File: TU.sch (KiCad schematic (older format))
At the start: 5 parts, among them J1 Conn_01x06_Male, J2 Conn_01x17_Male, J3 Conn_Coaxial, J4 Debugger connector, J7 Conn_Coaxial

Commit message: More routing changes
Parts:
- removed J3, J7: Conn_Coaxial, Connector_Coaxial:SMA_Amphenol_132134-10_Vertical, symbol Connector:Conn_Coaxial
- added J3, J6: Conn_01x05_Male, TU-HW RF LIB:Wurth_SMA_60312002114503, symbol Connector:Conn_01x05_Male
- added R18: 0, Resistor_SMD:R_0603_1608Metric, symbol Device:R
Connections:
- net +5V: now also R18.1; no longer J2.5 (Pin_5)
- net CC1190/ANTENNA_OUT: now also J3.1 (Pin_1)
- net GND: now also J2.17 (Pin_17), J3.2 (Pin_2), J3.3 (Pin_3), J3.4 (Pin_4), J3.5 (Pin_5), J6.2 (Pin_2), J6.3 (Pin_3), J6.4 (Pin_4), J6.5 (Pin_5)
- net GPIO2: now reaches J4.3 (Pin_3)
- net GPIO0: now reaches J4.4 (Pin_4)
- net at J2.1 (Pin_1): now also J6.1 (Pin_1)
- net ~RESET_RF2: now reaches J2.14 (Pin_14)
- net DIO5: now reaches J2.15 (Pin_15)
- net DIO3: now reaches J2.3 (Pin_3)
- net DIO4: now reaches J2.4 (Pin_4)
- net DIO0: now reaches J2.6 (Pin_6)
- net DIO1: now reaches J2.7 (Pin_7)
- net DIO2: now reaches J2.8 (Pin_8)
- net MCU/MISO renamed MISO
- net MISO: no longer J2.10 (Pin_10)
- net MCU/MOSI renamed MOSI
- net MOSI: no longer J2.11 (Pin_11)
- net MCU/SLCK renamed SCLK
- net SCLK: no longer J2.12 (Pin_12)
- net MCU/~CS_2 renamed ~CS_1
- net ~CS_1: no longer J2.13 (Pin_13)
- net transceiver/~RESET renamed ~RESET
- new net: J2.5 (Pin_5), R18.2
- new net MISO_RF2: J2.10 (Pin_10)
- new net MOSI_RF2: J2.11 (Pin_11)
- new net SCLK_RF2: J2.12 (Pin_12)
- new net ~CS_RF2: J2.13 (Pin_13)
- no-connect marks 10 -> 1
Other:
- note removed: "Piggyback backup rf module"
- moved on the sheet: J2

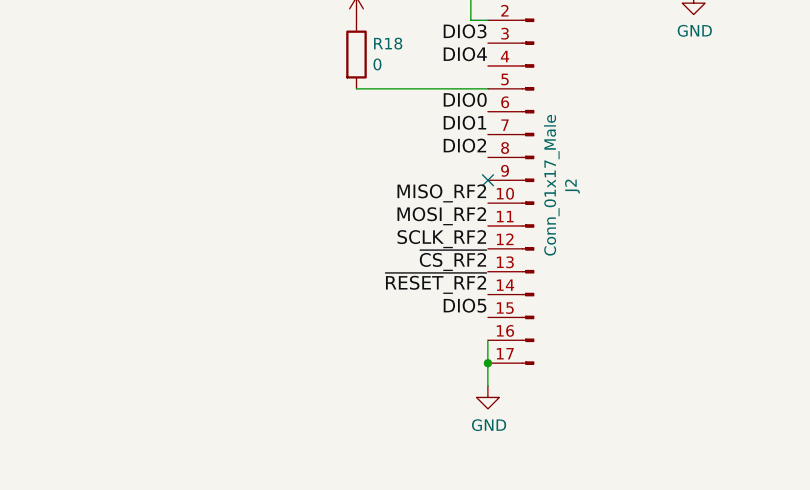
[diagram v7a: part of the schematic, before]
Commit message: Added edge cuts and silk screen comments
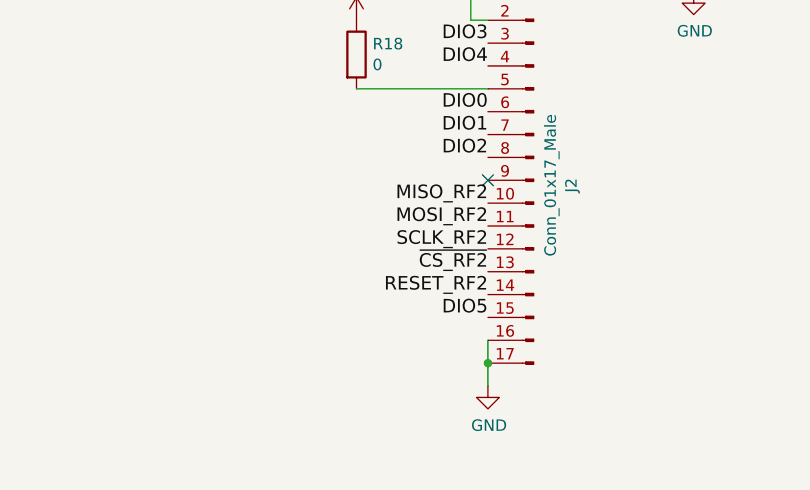
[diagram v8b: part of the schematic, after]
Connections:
- net ~RESET_RF2 is gone; now on net RESET_RF2: J2.14 (Pin_14)
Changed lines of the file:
@@
 SCLK_RF2
 Text Label 9050 5250 2    59   ~ 0
-~RESET_RF2
+RESET_RF2
 Text Label 9050 5350 2    59   ~ 0
 DIO5
